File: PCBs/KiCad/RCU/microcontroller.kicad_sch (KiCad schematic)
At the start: 24 parts, among them J200 USB_C_Receptacle_USB2.0, J201 Conn_01x05, SW201 SW_Push, U200 STM32G0B1CBT6, U201 USBLC6-2SC6, Y200 16MHz

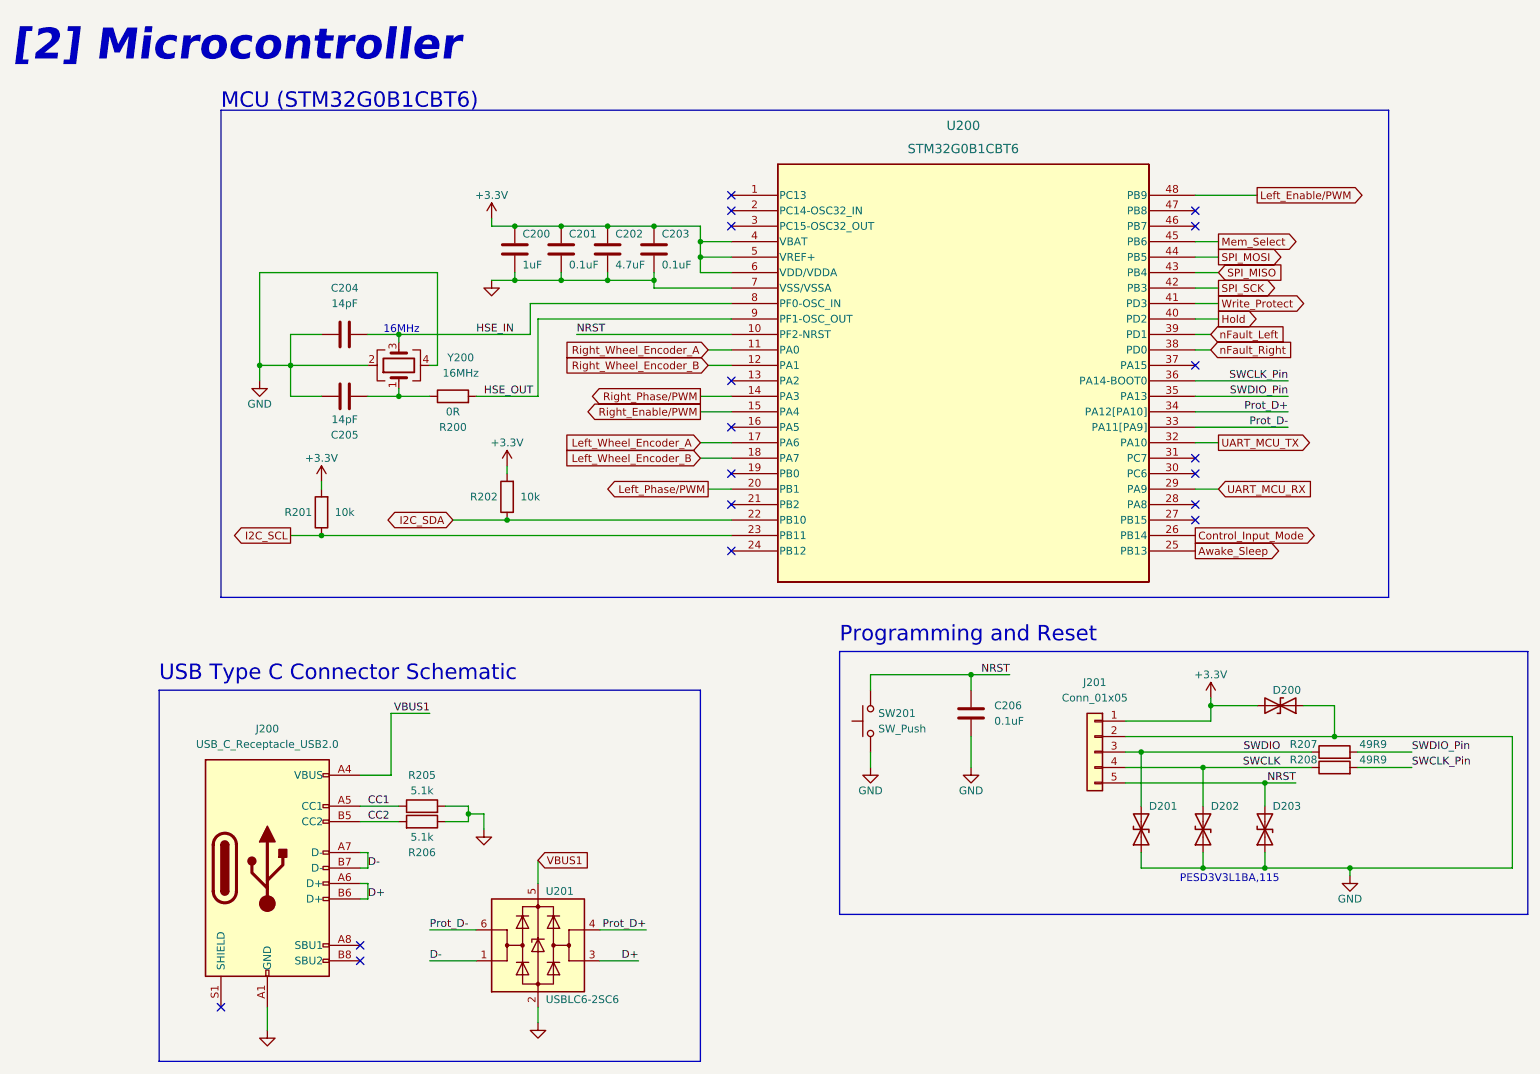
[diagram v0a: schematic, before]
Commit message: Moved project library one folder up to Kicad Folder
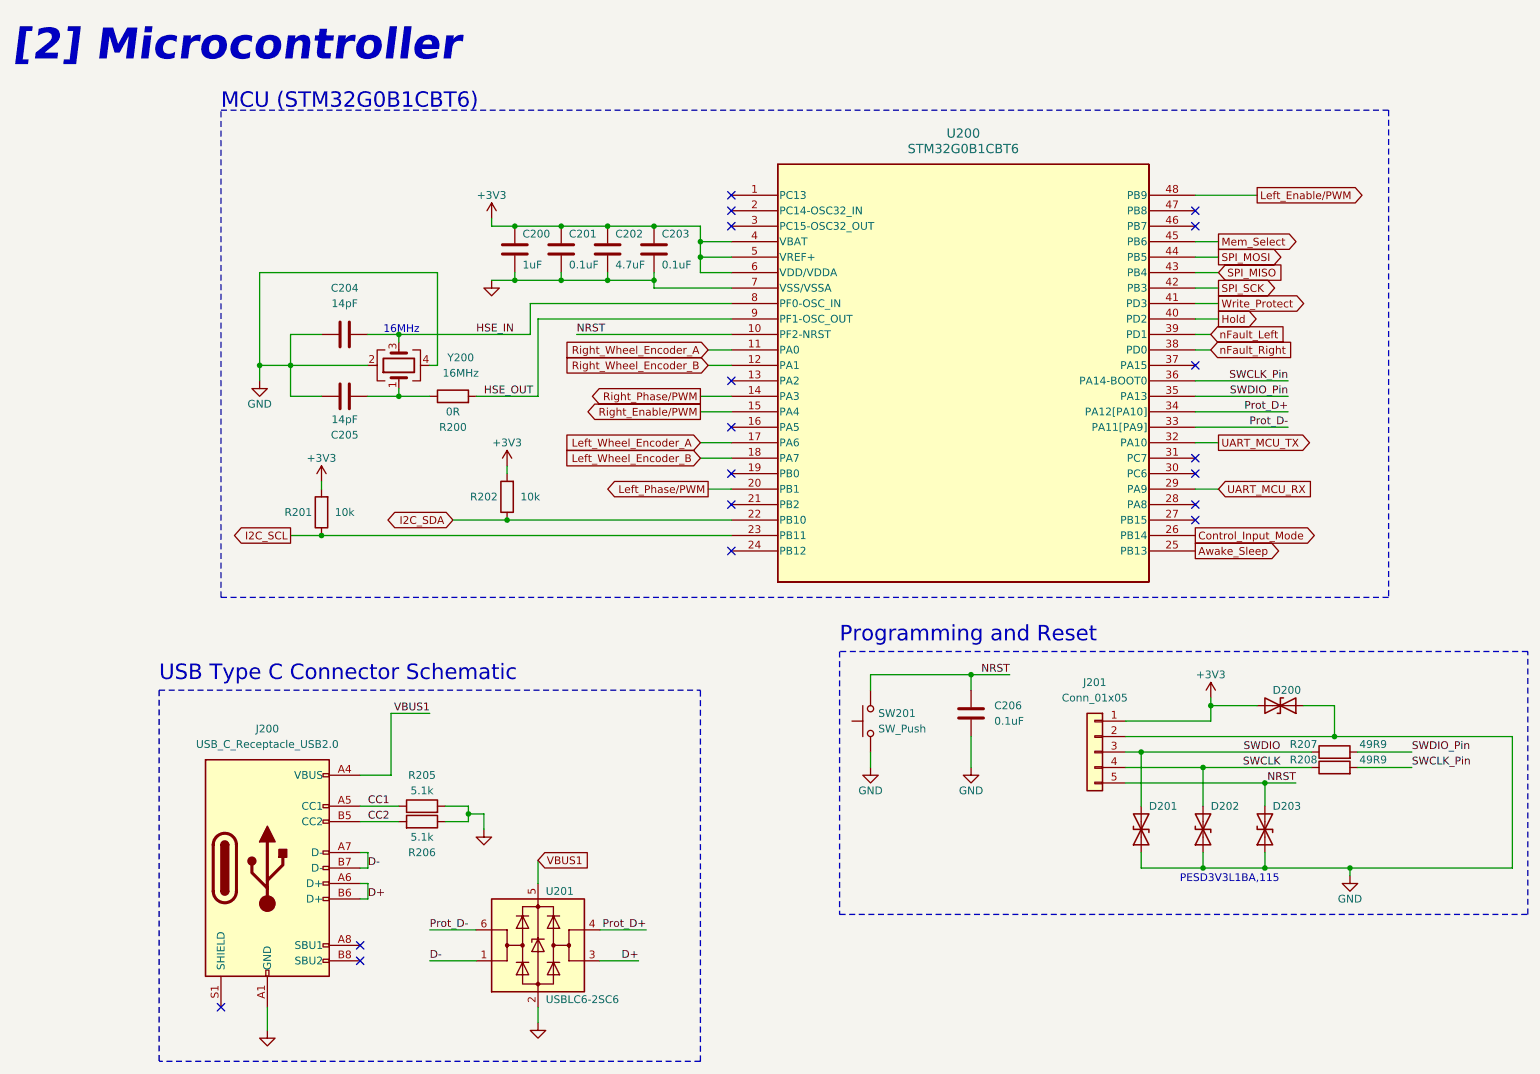
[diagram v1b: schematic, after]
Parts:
- removed U200: STM32G0B1CBT6, Package_QFP:LQFP-48_7x7mm_P0.5mm, symbol 2024-04-19_01-31-40:STM32G0B1CBT6
- added U200: STM32G0B1CBT6, Package_QFP:LQFP-48-1EP_7x7mm_P0.5mm_EP3.6x3.6mm, symbol STM32G0B1CBT6:STM32G0B1CBT6
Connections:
- net +3V3: now also U200.4 (VBAT), U200.5 (VREF+), U200.6 (VDD/VDDA)
- net Awake_Sleep: now also U200.25 (PB13)
- net Control_Input_Mode: now also U200.26 (PB14)
- net GND: now also U200.7 (VSS/VSSA)
- net HSE_IN: now also U200.8 (PF0-OSC_IN)
- net HSE_OUT: now also U200.9 (PF1-OSC_OUT)
- net Hold: now also U200.40 (PD2)
- net I2C_SCL: now also U200.23 (PB11)
- net I2C_SDA: now also U200.22 (PB10)
- net Left_Enable/PWM: now also U200.48 (PB9)
- net Left_Phase/PWM: now also U200.20 (PB1)
- net Left_Wheel_Encoder_A: now also U200.17 (PA6)
- net Left_Wheel_Encoder_B: now also U200.18 (PA7)
- net Mem_Select: now also U200.45 (PB6)
- net NRST: now also U200.10 (PF2-NRST)
- net Prot_D+: now also U200.34 (PA12[PA10])
- net Prot_D-: now also U200.33 (PA11[PA9])
- net Right_Enable/PWM: now also U200.15 (PA4)
- net Right_Phase/PWM: now also U200.14 (PA3)
- net Right_Wheel_Encoder_A: now also U200.11 (PA0)
- net Right_Wheel_Encoder_B: now also U200.12 (PA1)
- net SPI_MISO: now also U200.43 (PB4)
- net SPI_MOSI: now also U200.44 (PB5)
- net SPI_SCK: now also U200.42 (PB3)
- net SWCLK_Pin: now also U200.36 (PA14-BOOT0)
- net SWDIO_Pin: now also U200.35 (PA13)
- net UART_MCU_RX: now also U200.29 (PA9)
- net UART_MCU_TX: now also U200.32 (PA10)
- net Write_Protect: now also U200.41 (PD3)
- net nFault_Left: now also U200.39 (PD1)
- net nFault_Right: now also U200.38 (PD0)
